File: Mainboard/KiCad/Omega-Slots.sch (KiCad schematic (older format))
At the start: 8 parts, among them U14 ATF16V8B, U19 74F541, U20 74F541, U21 74F541, U25 74F245

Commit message: Mainboard: Fixed schematic and PCB for v1.1
Signed-off-by: Sergey Kiselev <skiselev@gmail.com>
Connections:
- wire segments 265 -> 263
- no-connect marks 1 -> 3

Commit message: Mainboard: Fix some of the issues described in #1
Signed-off-by: Sergey Kiselev <skiselev@gmail.com>
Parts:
- U19, U20, U21: symbol Omega-Mainboard-rescue:74LS541-my_components -> 74xx:74LS541
- U25: symbol my_components:74LS245 -> 74xx:74LS245
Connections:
- wire segments 263 -> 275
- no-connect marks 3 -> 1
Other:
- moved on the sheet: RR4, U14

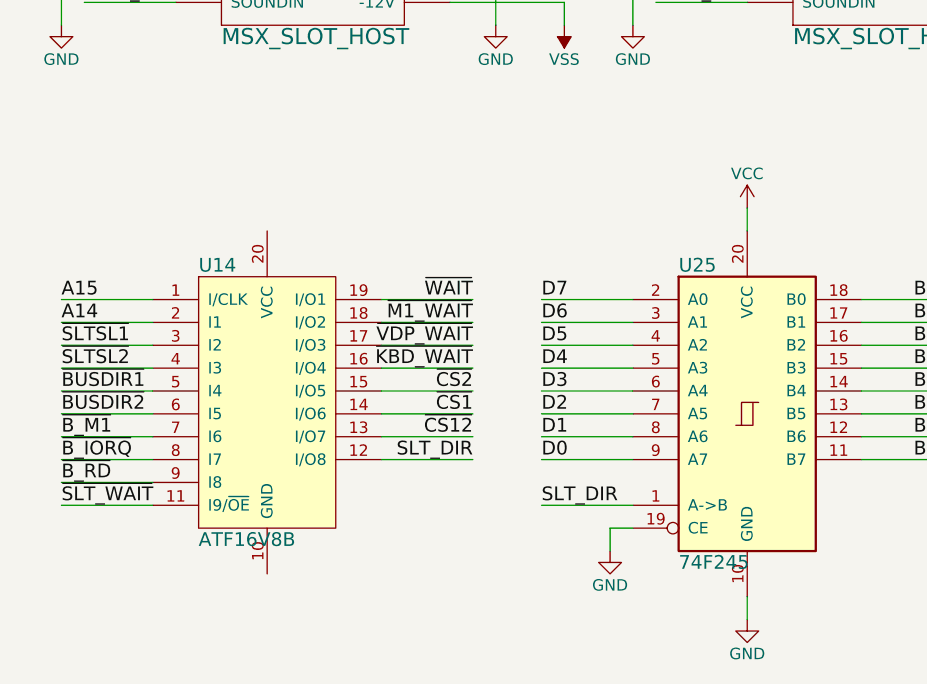
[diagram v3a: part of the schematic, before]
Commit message: Mainboard: Swap slots, use trmp cap for RTC, add color bus
Signed-off-by: Sergey Kiselev <skiselev@gmail.com>
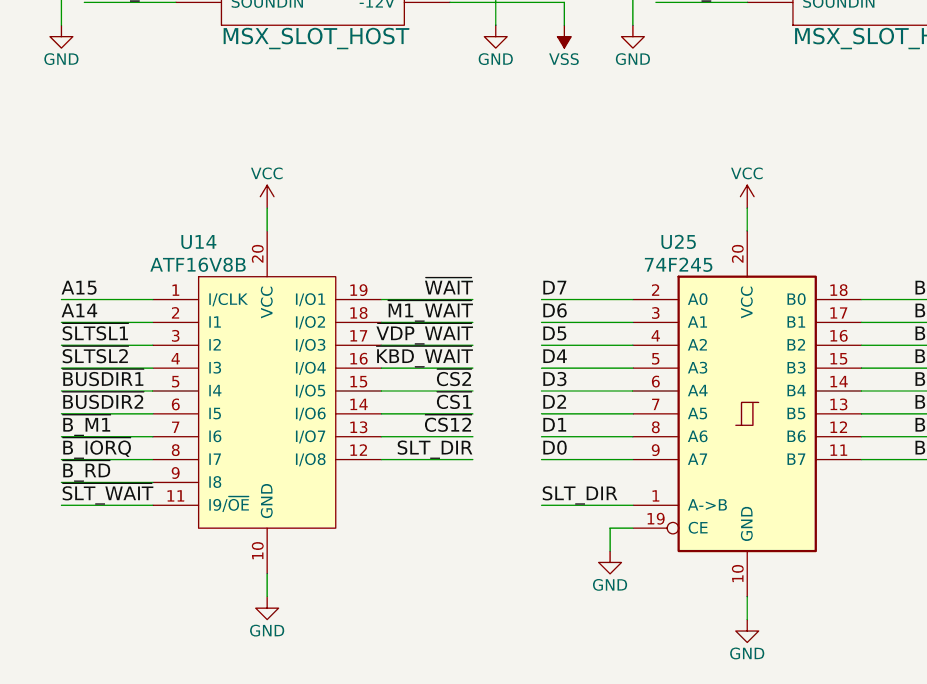
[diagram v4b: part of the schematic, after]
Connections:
- net GND: now also U14.10 (GND)
- net VCC: now also U14.20 (VCC)
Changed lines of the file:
@@
 U 1 1 5BEF3954
 P 3800 5100
-F 0 "U25" H 3500 5750 60  0000 L CNN
-F 1 "74F245" H 3500 4450 60  0000 L CNN
+F 0 "U25" H 3500 5850 60  0000 C CNN
+F 1 "74F245" H 3500 5750 60  0000 C CNN
 F 2 "My_Components:IC_DIP20_300" H 3800 5100 60  0001 C CNN
 F 3 "" H 3800 5100 60  0000 C CNN
@@
 Text Label 10200 3200 0    60   ~ 0
 SLT2_SND
-Text Label 9100 3200 0    60   ~ 0
-~BUSDIR1
 Text Label 9100 3300 0    60   ~ 0
 ~BUSDIR2
@@
 U 1 1 5C015547
 P 1700 5050
-F 0 "U14" H 1400 5650 60  0000 L CNN
-F 1 "ATF16V8B" H 1400 4450 60  0000 L CNN
+F 0 "U14" H 1400 5750 60  0000 C CNN
+F 1 "ATF16V8B" H 1400 5650 60  0000 C CNN
 F 2 "My_Components:IC_DIP20_300" H 1700 4950 60  0001 C CNN
 F 3 "" H 1700 4950 60  0000 C CNN
@@
 Wire Wire Line
 	5200 3100 5200 3400
+$Comp
+L power:VCC #PWR0158
+U 1 1 5FB580C1
+P 1700 4200
+F 0 "#PWR0158" H 1700 4050 50  0001 C CNN
+F 1 "VCC" H 1700 4350 50  0000 C CNN
+F 2 "" H 1700 4200 50  0001 C CNN
+F 3 "" H 1700 4200 50  0001 C CNN
+	1    1700 4200
+	1    0    0    -1
+$EndComp
+Wire Wire Line
+	1700 4300 1700 4200
+Wire Wire Line
+	1700 5800 1700 5900
+$Comp
+L power:GND #PWR0159
+U 1 1 5FB7E620
+P 1700 5900
+F 0 "#PWR0159" H 1700 5650 50  0001 C CNN
+F 1 "GND" H 1700 5750 50  0000 C CNN
+F 2 "" H 1700 5900 50  0001 C CNN
+F 3 "" H 1700 5900 50  0001 C CNN
+	1    1700 5900
+	1    0    0    -1
+$EndComp
+Text Label 9100 3200 0    60   ~ 0
+~BUSDIR1
 $EndSCHEMATC

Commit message: Add files for version 1.3eu from Jordi Solis
Signed-off-by: Sergey Kiselev <skiselev@gmail.com>
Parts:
- RR4: symbol my_components:RR9 -> Omega-Mainboard-rescue:RR9-my_components
- SLOT1, SLOT2: symbol my_components:MSX_SLOT_HOST -> Omega-Mainboard-rescue:MSX_SLOT_HOST-my_components
- U14: symbol my_components:ATF16V8B -> Omega-Mainboard-rescue:ATF16V8B-my_components
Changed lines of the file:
@@
 EESchema Schematic File Version 4
 LIBS:Omega-Mainboard-cache
-EELAYER 29 0
+EELAYER 30 0
 EELAYER END
 $Descr A4 11693 8268
@@
 $EndDescr
 $Comp
-L my_components:MSX_SLOT_HOST SLOT1
+L Omega-Mainboard-rescue:MSX_SLOT_HOST-my_components SLOT1
 U 1 1 5BEF23EE
 P 1900 2100
@@
 SLT1_SND
 $Comp
-L my_components:MSX_SLOT_HOST SLOT2
+L Omega-Mainboard-rescue:MSX_SLOT_HOST-my_components SLOT2
 U 1 1 5BEF246E
 P 4400 2100
@@
 	1300 900  900  900
 $Comp
-L my_components:RR9 RR4
+L Omega-Mainboard-rescue:RR9-my_components RR4
 U 1 1 5BEF9034
 P 7200 2350
@@
 ~BUSDIR2
 $Comp
-L my_components:ATF16V8B U14
+L Omega-Mainboard-rescue:ATF16V8B-my_components U14
 U 1 1 5C015547
 P 1700 5050

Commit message: Version 1.4: Add cut-out for the right angle slot connector. Add optional jumpers to limit memory mapper address range
Signed-off-by: Sergey Kiselev <skiselev@gmail.com>
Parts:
- RR4: symbol Omega-Mainboard-rescue:RR9-my_components -> my_components:RR9
- SLOT1, SLOT2: symbol Omega-Mainboard-rescue:MSX_SLOT_HOST-my_components -> my_components:MSX_SLOT_HOST
- U14: symbol Omega-Mainboard-rescue:ATF16V8B-my_components -> my_components:ATF16V8B
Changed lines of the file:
@@
 EESchema Schematic File Version 4
-LIBS:Omega-Mainboard-cache
 EELAYER 30 0
 EELAYER END
@@
 $EndDescr
 $Comp
-L Omega-Mainboard-rescue:MSX_SLOT_HOST-my_components SLOT1
+L my_components:MSX_SLOT_HOST SLOT1
 U 1 1 5BEF23EE
 P 1900 2100
@@
 SLT1_SND
 $Comp
-L Omega-Mainboard-rescue:MSX_SLOT_HOST-my_components SLOT2
+L my_components:MSX_SLOT_HOST SLOT2
 U 1 1 5BEF246E
 P 4400 2100
@@
 	1300 900  900  900
 $Comp
-L Omega-Mainboard-rescue:RR9-my_components RR4
+L my_components:RR9 RR4
 U 1 1 5BEF9034
 P 7200 2350
@@
 ~BUSDIR2
 $Comp
-L Omega-Mainboard-rescue:ATF16V8B-my_components U14
+L my_components:ATF16V8B U14
 U 1 1 5C015547
 P 1700 5050
